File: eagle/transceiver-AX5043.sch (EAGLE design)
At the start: 41 parts, among them J1 142-0701-851, J2 142-0701-851, J3 142-0701-851, Q1 PMOS, U1 U-ONSEMI-AX5043, X1 TAITIEN-TY

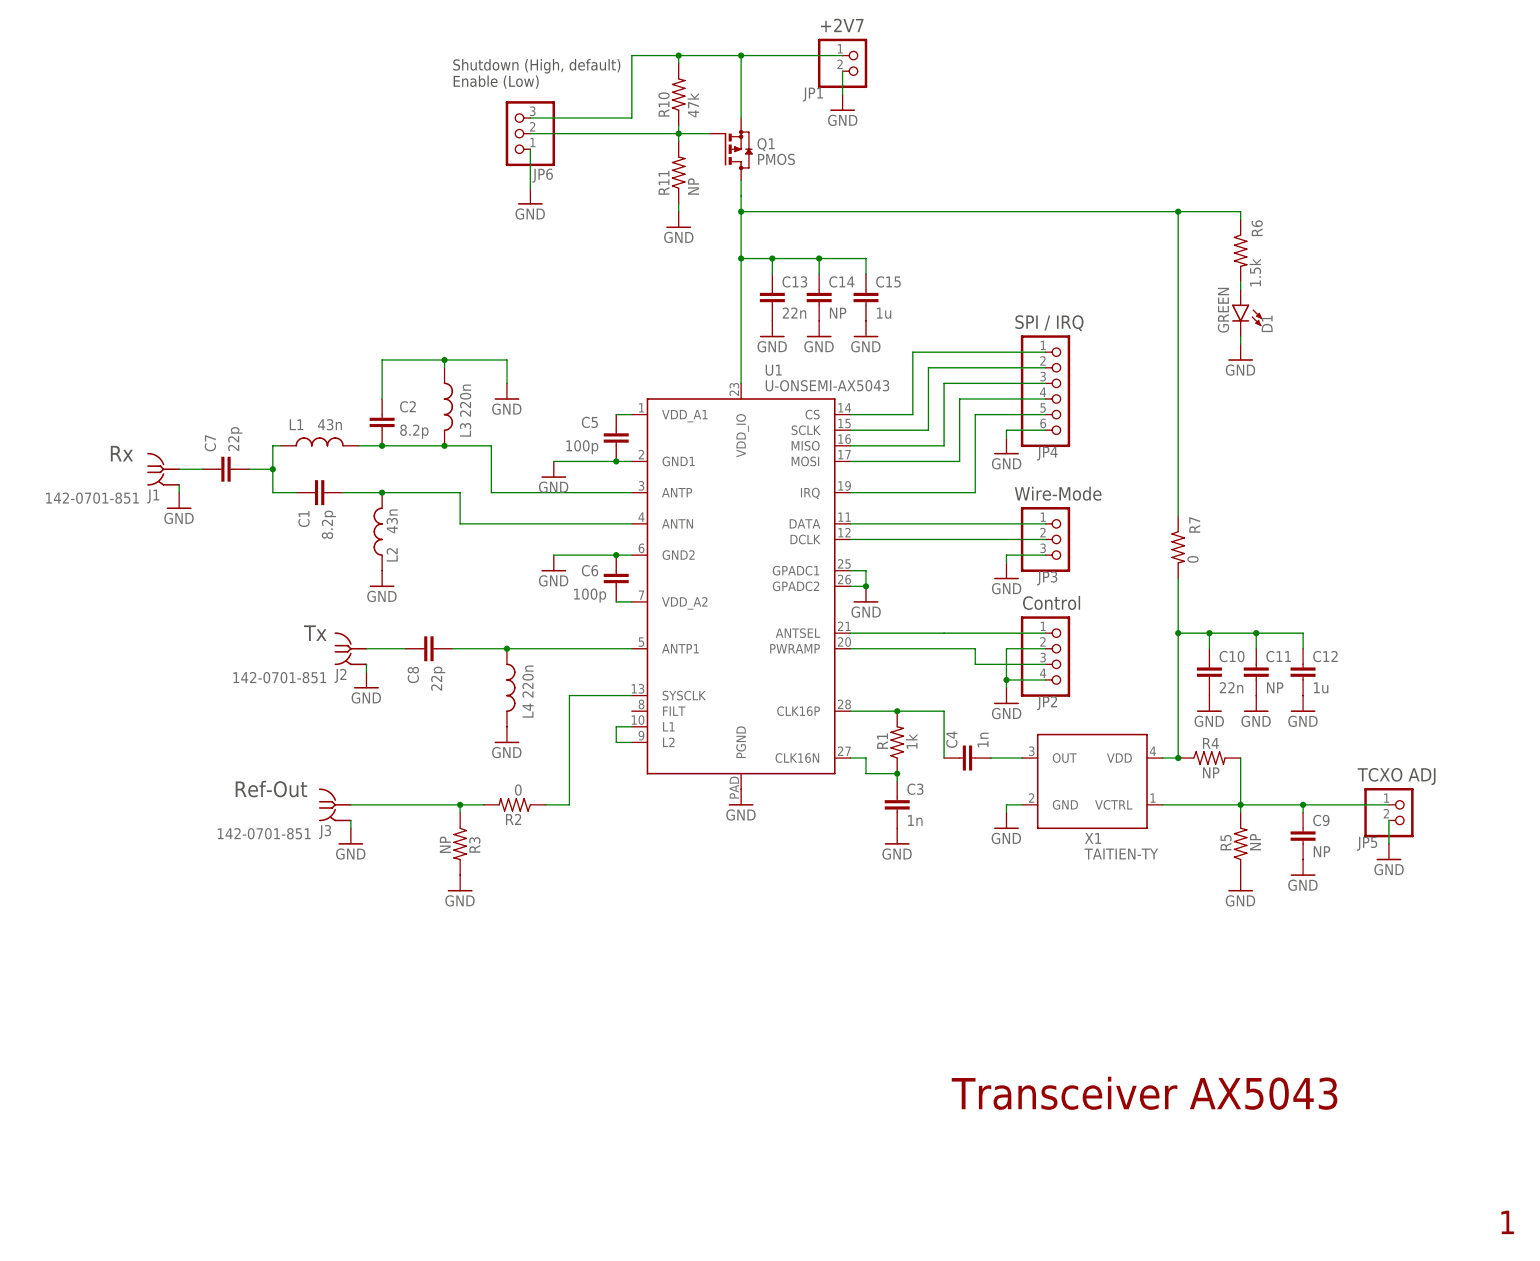
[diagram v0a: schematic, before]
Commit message: Finish AX5043 schematic
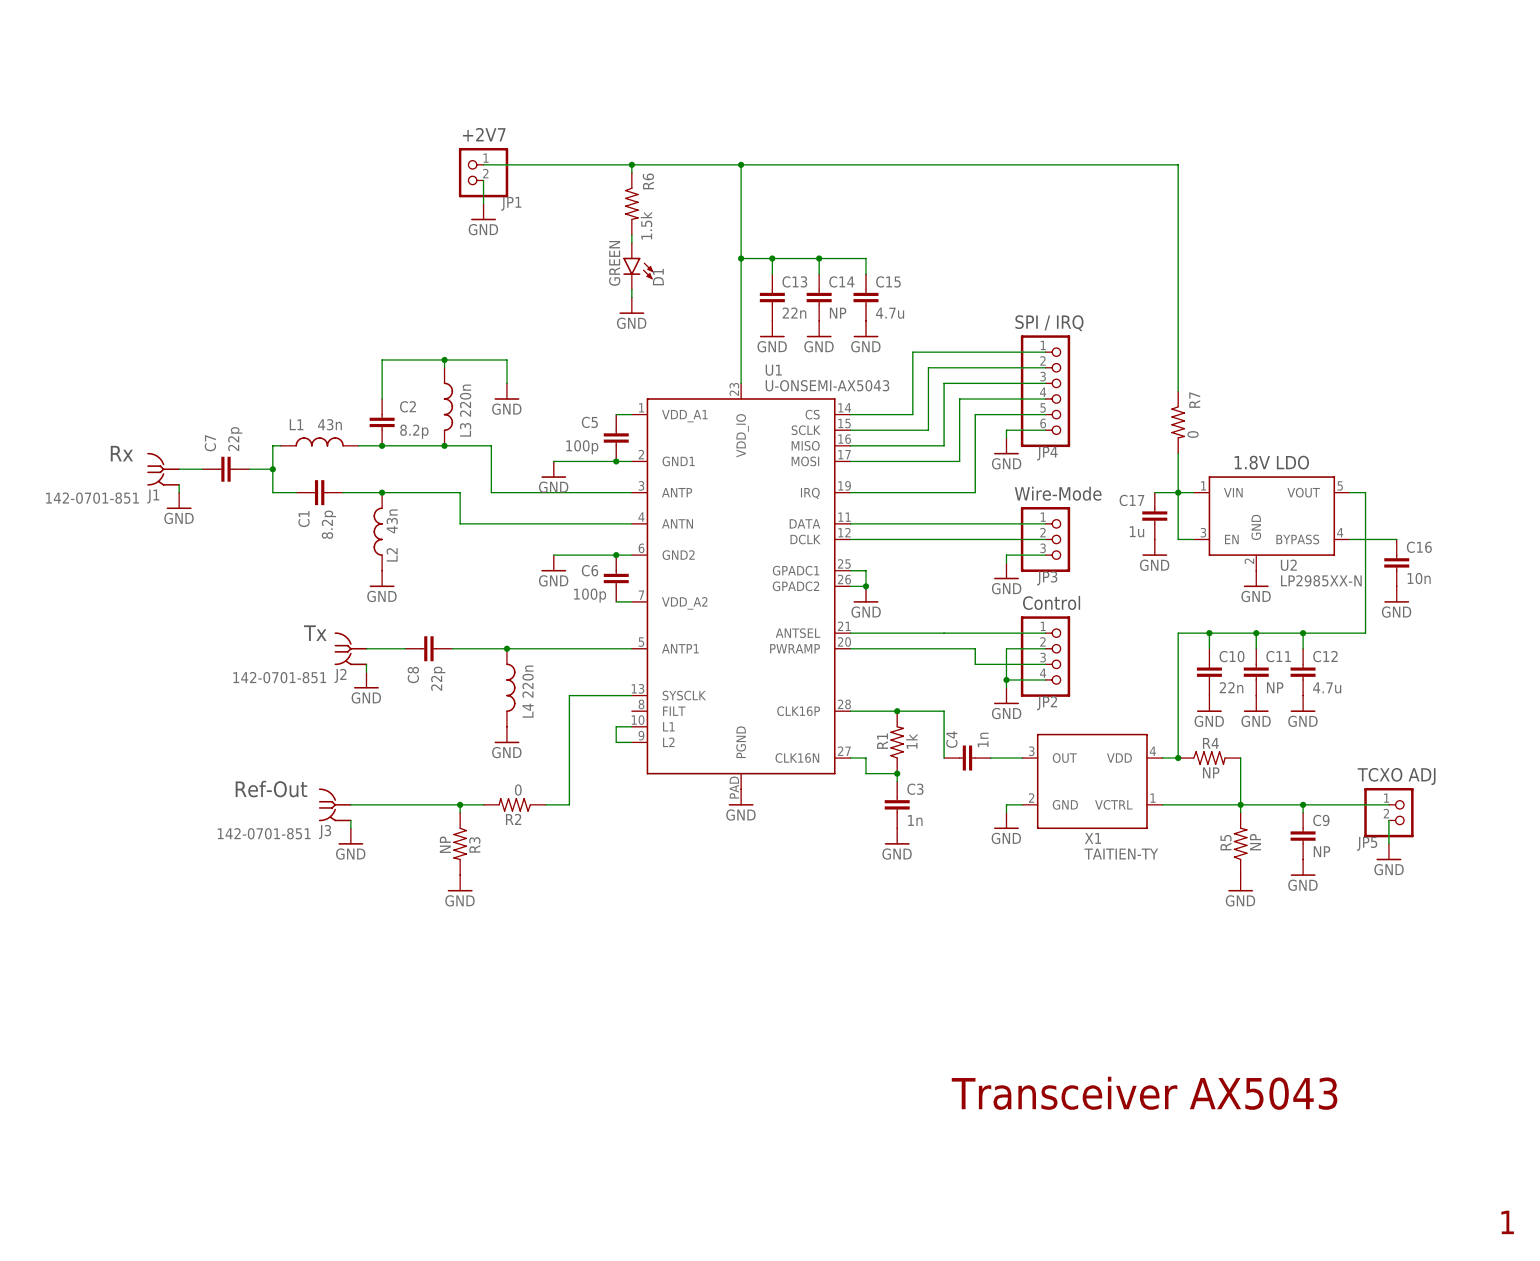
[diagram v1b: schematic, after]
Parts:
- removed JP6: (no value), pinhead:PINHD-1X3
- removed Q1: PMOS, transistor-small-signal:BSS84
- removed R10: 47k, oresat-rcl:R-US_0402-B-NOSILK
- removed R11: NP, oresat-rcl:R-US_0402-B-NOSILK
- added C16: 10n, oresat-rcl:C-EU0603-C-NOSILK
- added C17: 1u, oresat-rcl:C-EU0603-C-NOSILK
- added U2: LP2985XX-N, U-TI-LP2985XX-N-linear-reg:LP2985XX-N
- C12, C15: value 1u -> 4.7u
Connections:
- removed net N$28: JP1.1, JP6.3, Q1.S, R10.2
- new net N$2: C17.1, R7.2, U2.EN, U2.VIN
- net GND: now also C16.2, C17.2, U2.GND; no longer JP6.1, R11.1
- net N$24: now also U2.VOUT; no longer R7.2
- net N$25: now also JP1.1; no longer Q1.D
- net N$27: now also C16.1, U2.BYPASS; no longer JP6.2, Q1.G, R10.1, R11.2
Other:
- note added: "1.8V LDO"
- note removed: "Shutdown (High, default) Enable (Low)"
- moved on the sheet: D1, JP1, R6, R7

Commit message: Add initial layout AX5043
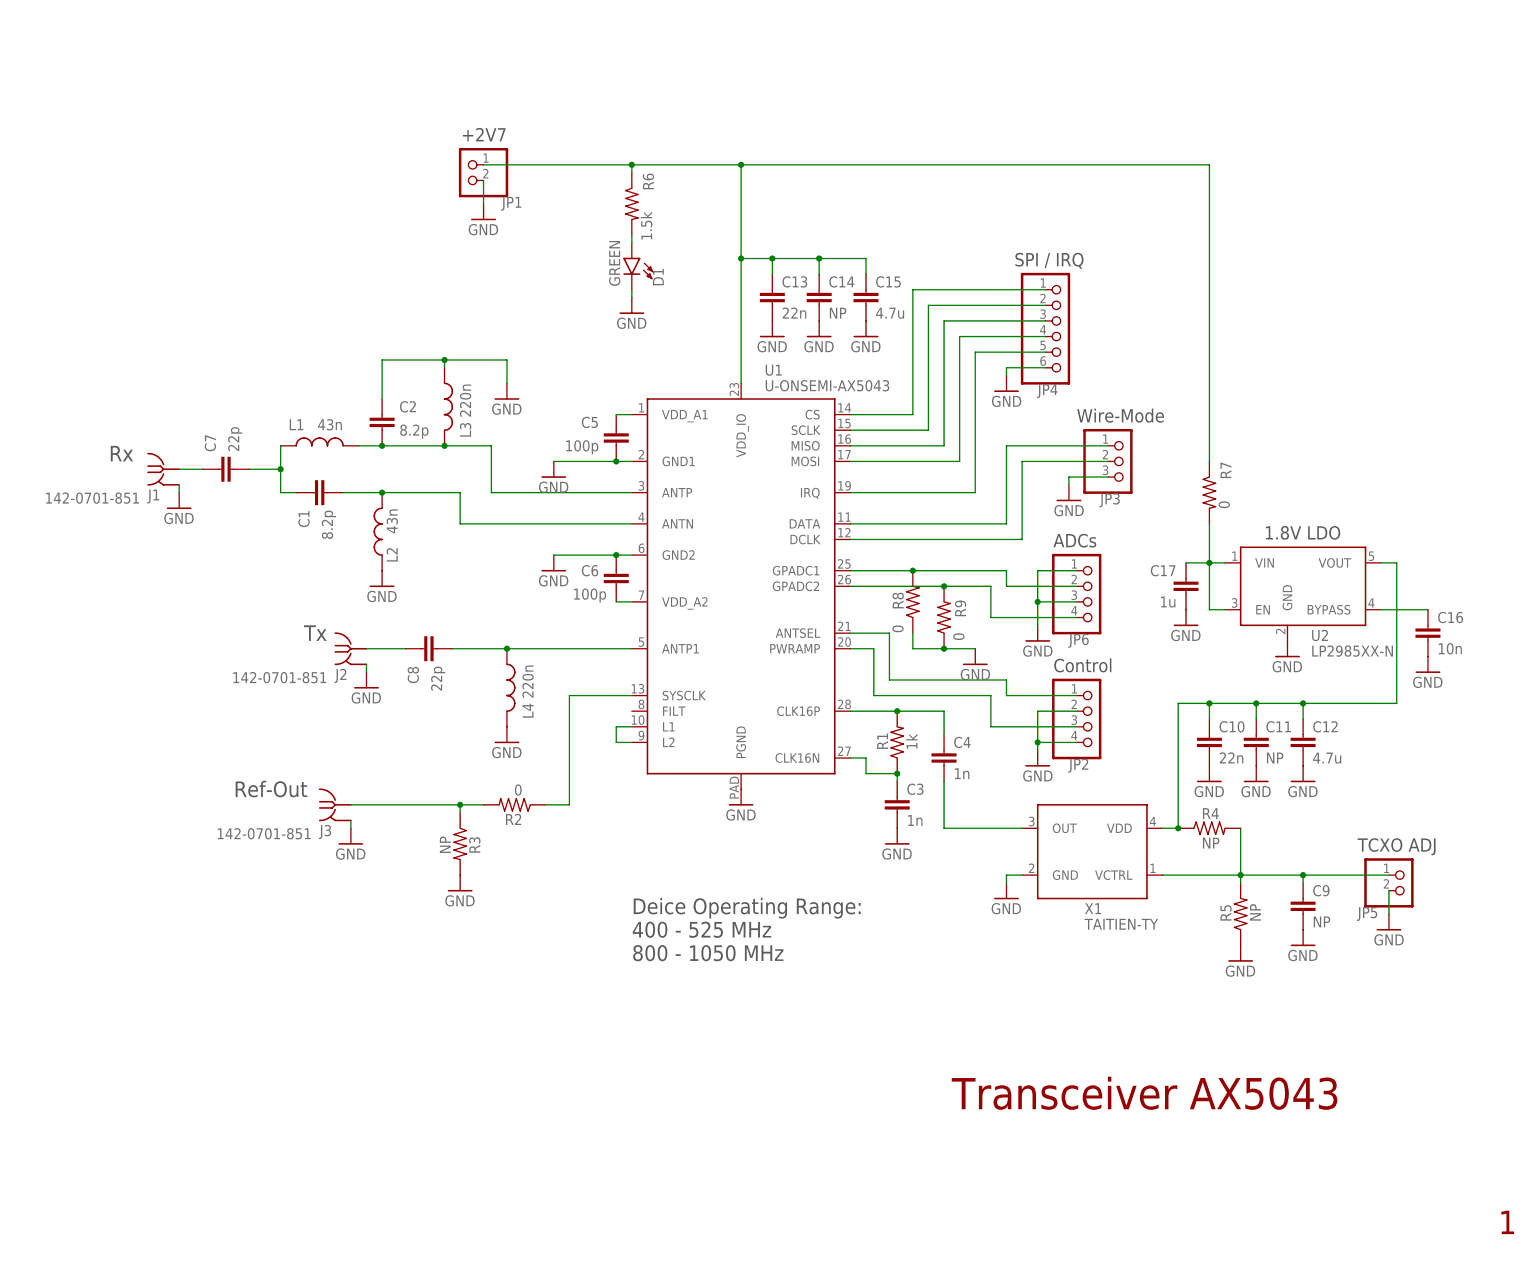
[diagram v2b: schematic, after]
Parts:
- added JP6: (no value), pinhead:PINHD-1X4
- added R8, R9: 0, oresat-rcl:R-US_0402-C-NOSILK
- L1, L2: device oresat-rcl:L-US0603-C-NOSILK -> oresat-rcl:L-US0402-C-NOSILK
- L4: device oresat-rcl:L-US0402-C-NOSILK -> oresat-rcl:L-US0603-C-NOSILK
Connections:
- net N$14 renamed CLKN
- net N$15 renamed CLKP
- net N$17 renamed ANTN
- net N$18 renamed ANTP
- net N$19 renamed ANTP1
- net N$20 renamed TX
- net N$22 renamed REF-OUT
- net N$24 renamed 1V8
- net N$25 renamed 2V7
- net N$4 renamed SYSCLK
- removed net N$21: C7.1, J1.RF
- new net N$20: C1.1, C7.2, L1.1
- new net N$4: JP6.2, R8.2, U1.GPADC1
- new net N$5: JP6.4, R9.2, U1.GPADC2
- net GND: now also JP6.1, JP6.3, R8.1, R9.1; no longer U1.GPADC1, U1.GPADC2
- net RX: now also C7.1, J1.RF; no longer C1.1, C7.2, L1.1
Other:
- note added: "ADCs"
- note added: "Deice Operating Range: 400 - 525 MHz 800 - 1050 MHz"
- moved on the sheet: C10, C11, C12, C16, C17, C4, C9, JP2, JP3, JP4, JP5, R4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

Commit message: Update layout AX5043
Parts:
- R7: device oresat-rcl:R-US_0603-B-NOSILK -> oresat-rcl:R-US_0603-C-NOSILK
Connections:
- net N$14: now also JP3.2; no longer JP3.1
- net N$15: now also JP3.1; no longer JP3.2
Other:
- note added: "Device Operating Range: 400 - 525 MHz 800 - 1050 MHz"
- note removed: "Deice Operating Range: 400 - 525 MHz 800 - 1050 MHz"
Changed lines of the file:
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@@
 <class number="0" name="default" width="0" drill="0">
+</class>
+<class number="1" name="RF1" width="0" drill="0">
+<clearance class="1" value="0.8"/>
+</class>
+<class number="2" name="RF2" width="0" drill="0">
+<clearance class="2" value="0.4"/>
 </class>
 </classes>
@@
 <part name="GND80" library="supply1" deviceset="GND" device=""/>
 <part name="R6" library="oresat-rcl" deviceset="R-US_" device="0603-B-NOSILK" value="1.5k"/>
-<part name="R7" library="oresat-rcl" deviceset="R-US_" device="0603-B-NOSILK" value="0"/>
+<part name="R7" library="oresat-rcl" deviceset="R-US_" device="0603-C-NOSILK" value="0"/>
 <part name="GND14" library="supply1" library_urn="urn:adsk.eagle:library:371" deviceset="GND" device=""/>
 <part name="U2" library="U-TI-LP2985XX-N-linear-reg" deviceset="LP2985XX-N" device=""/>
@@
 <text x="227.33" y="119.38" size="2.159" layer="97">1.8V LDO</text>
 <text x="193.04" y="118.11" size="2.159" layer="97">ADCs</text>
-<text x="124.46" y="50.8" size="2.54" layer="97">Deice Operating Range:
+<text x="121.92" y="45.72" size="2.54" layer="97">Device Operating Range:
 400 - 525 MHz
 800 - 1050 MHz</text>
@@
 </segment>
 </net>
-<net name="TX" class="0">
+<net name="TX" class="1">
 <segment>
 <pinref part="J2" gate="G$1" pin="RF"/>
@@
 </segment>
 </net>
-<net name="RX" class="0">
+<net name="RX" class="1">
 <segment>
 <pinref part="J1" gate="G$1" pin="RF"/>
@@
 </segment>
 </net>
-<net name="REF-OUT" class="0">
+<net name="REF-OUT" class="1">
 <segment>
 <pinref part="J3" gate="G$1" pin="RF"/>
@@
 </segment>
 </net>
-<net name="N$20" class="0">
+<net name="N$20" class="2">
 <segment>
 <pinref part="C7" gate="CE" pin="2"/>
@@
 </segment>
 </net>
-<net name="N$6" class="0">
+<net name="N$6" class="2">
 <segment>
 <pinref part="C4" gate="CE" pin="2"/>
@@
 <net name="N$14" class="0">
 <segment>
-<pinref part="JP3" gate="A" pin="1"/>
-<wire x1="201.93" y1="134.62" x2="185.42" y2="134.62" width="0.1524" layer="91"/>
-<wire x1="185.42" y1="134.62" x2="185.42" y2="121.92" width="0.1524" layer="91"/>
 <pinref part="U1" gate="G$1" pin="DATA"/>
 <wire x1="185.42" y1="121.92" x2="160.02" y2="121.92" width="0.1524" layer="91"/>
+<pinref part="JP3" gate="A" pin="2"/>
+<wire x1="185.42" y1="121.92" x2="185.42" y2="132.08" width="0.1524" layer="91"/>
+<wire x1="185.42" y1="132.08" x2="201.93" y2="132.08" width="0.1524" layer="91"/>
 </segment>
 </net>
@@
 <pinref part="U1" gate="G$1" pin="DCLK"/>
 <wire x1="160.02" y1="119.38" x2="187.96" y2="119.38" width="0.1524" layer="91"/>
-<wire x1="187.96" y1="119.38" x2="187.96" y2="132.08" width="0.1524" layer="91"/>
-<pinref part="JP3" gate="A" pin="2"/>
-<wire x1="187.96" y1="132.08" x2="201.93" y2="132.08" width="0.1524" layer="91"/>
-</segment>
-</net>
+<pinref part="JP3" gate="A" pin="1"/>
+<wire x1="187.96" y1="119.38" x2="187.96" y2="134.62" width="0.1524" layer="91"/>
+<wire x1="187.96" y1="134.62" x2="201.93" y2="134.62" width="0.1524" layer="91"/>
+</segment>
+</net>

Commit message: Finalized AX5043 layout
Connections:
- net N$10 renamed MOSI
- net N$11 renamed MISO
- net N$12 renamed SCLK
- net N$13 renamed CS
- net N$14 renamed DATA
- net N$15 renamed DCLK
- net N$4 renamed ADC1
- net N$5 renamed ADC2
- net N$7 renamed ANTSEL
- net N$8 renamed PWRAMP
- net N$9 renamed IRQ
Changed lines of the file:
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@@
 </segment>
 </net>
-<net name="N$9" class="0">
+<net name="IRQ" class="0">
 <segment>
 <pinref part="U1" gate="G$1" pin="IRQ"/>
@@
 </segment>
 </net>
-<net name="N$10" class="0">
+<net name="MOSI" class="0">
 <segment>
 <pinref part="U1" gate="G$1" pin="MOSI"/>
@@
 </segment>
 </net>
-<net name="N$11" class="0">
+<net name="MISO" class="0">
 <segment>
 <pinref part="U1" gate="G$1" pin="MISO"/>
@@
 </segment>
 </net>
-<net name="N$12" class="0">
+<net name="SCLK" class="0">
 <segment>
 <pinref part="U1" gate="G$1" pin="SCLK"/>
@@
 </segment>
 </net>
-<net name="N$13" class="0">
+<net name="CS" class="0">
 <segment>
 <pinref part="U1" gate="G$1" pin="CS"/>
@@
 </segment>
 </net>
-<net name="N$7" class="0">
+<net name="ANTSEL" class="0">
 <segment>
 <pinref part="JP2" gate="A" pin="1"/>
@@
 </segment>
 </net>
-<net name="N$8" class="0">
+<net name="PWRAMP" class="0">
 <segment>
 <pinref part="JP2" gate="A" pin="3"/>
@@
 </segment>
 </net>
-<net name="N$14" class="0">
+<net name="DATA" class="0">
 <segment>
 <pinref part="U1" gate="G$1" pin="DATA"/>
@@
 </segment>
 </net>
-<net name="N$15" class="0">
+<net name="DCLK" class="0">
 <segment>
 <pinref part="U1" gate="G$1" pin="DCLK"/>
@@
 </segment>
 </net>
-<net name="N$4" class="0">
+<net name="ADC1" class="0">
 <segment>
 <pinref part="U1" gate="G$1" pin="GPADC1"/>
@@
 </segment>
 </net>
-<net name="N$5" class="0">
+<net name="ADC2" class="0">
 <segment>
 <pinref part="U1" gate="G$1" pin="GPADC2"/>
